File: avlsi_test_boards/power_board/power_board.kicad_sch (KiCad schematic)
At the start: 4 parts, among them J1 PJ-102AH, J2 PJ-102AH, J3 Conn_02x06_Top_Bottom, J4 Conn_02x06_Top_Bottom

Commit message: Fully routed
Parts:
- removed J3, J4: Conn_02x06_Top_Bottom, Connector_PinHeader_2.54mm:PinHeader_2x06_P2.54mm_Vertical, symbol Connector_Generic:Conn_02x06_Top_Bottom
- added J3, J9: Conn_02x07_Top_Bottom, Connector_PinHeader_2.00mm:PinHeader_2x07_P2.00mm_Vertical, symbol Connector_Generic:Conn_02x07_Top_Bottom
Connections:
- net DGND: now also J9.1 (Pin_1), J9.11 (Pin_11), J9.13 (Pin_13), J9.3 (Pin_3), J9.5 (Pin_5), J9.7 (Pin_7), J9.9 (Pin_9)
- net VCCA09: now also J3.12 (Pin_12)
- net VCCA12: now also J3.10 (Pin_10)
- net VCCA18: now also J3.8 (Pin_8)
- net VCCA25: now also J3.6 (Pin_6)
- net VCCA33: now also J3.4 (Pin_4)
- net VCCD09: now also J9.4 (Pin_4)
- net VCCD12: now also J9.6 (Pin_6)
- net VCCD18: now also J9.8 (Pin_8)
- net VCCD25: now also J9.10 (Pin_10)
- net VCCD33: now also J9.12 (Pin_12)
- net AGND renamed ADGND
- net ADGND: now also J3.1 (Pin_1), J3.11 (Pin_11), J3.13 (Pin_13), J3.3 (Pin_3), J3.5 (Pin_5), J3.7 (Pin_7), J3.9 (Pin_9)
- net AVIN renamed AVIN5
- net AVIN5: now also J3.2 (Pin_2)
- net DVIN renamed DVIN5
- net DVIN5: now also J9.14 (Pin_14)
- new net VACustom: J3.14 (Pin_14)
- new net VDCustom: J9.2 (Pin_2)
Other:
- sheet analog_power_converters ports: added DGND; removed GND
- sheet digital_power_converters ports: added DGND; removed GND

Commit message: Add partial changes
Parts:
- removed J3, J9: Conn_02x07_Top_Bottom, Connector_PinHeader_2.00mm:PinHeader_2x07_P2.00mm_Vertical, symbol Connector_Generic:Conn_02x07_Top_Bottom
- added J3, J7: Conn_02x07_Odd_Even, Connector_PinHeader_2.54mm:PinHeader_2x07_P2.54mm_Vertical, symbol Connector_Generic:Conn_02x07_Odd_Even
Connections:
- net ADGND: now also J3.10 (Pin_10), J3.12 (Pin_12), J3.14 (Pin_14), J3.2 (Pin_2), J3.4 (Pin_4), J3.6 (Pin_6), J3.8 (Pin_8)
- net AVIN5: now also J3.13 (Pin_13)
- net DGND: now also J7.10 (Pin_10), J7.12 (Pin_12), J7.14 (Pin_14), J7.2 (Pin_2), J7.4 (Pin_4), J7.6 (Pin_6), J7.8 (Pin_8)
- net DVIN5: now also J7.13 (Pin_13)
- net VACustom: now also J3.1 (Pin_1)
- net VCCA09: now also J3.3 (Pin_3)
- net VCCA12: now also J3.5 (Pin_5)
- net VCCA18: now also J3.7 (Pin_7)
- net VCCA25: now also J3.9 (Pin_9)
- net VCCA33: now also J3.11 (Pin_11)
- net VCCD09: now also J7.3 (Pin_3)
- net VCCD12: now also J7.5 (Pin_5)
- net VCCD18: now also J7.7 (Pin_7)
- net VCCD25: now also J7.9 (Pin_9)
- net VCCD33: now also J7.11 (Pin_11)
- net VDCustom: now also J7.1 (Pin_1)
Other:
- added sheet level_shifter (level_shifter.kicad_sch)
- added sheet opal_kelly_connector (opal_kelly_connector.kicad_sch)

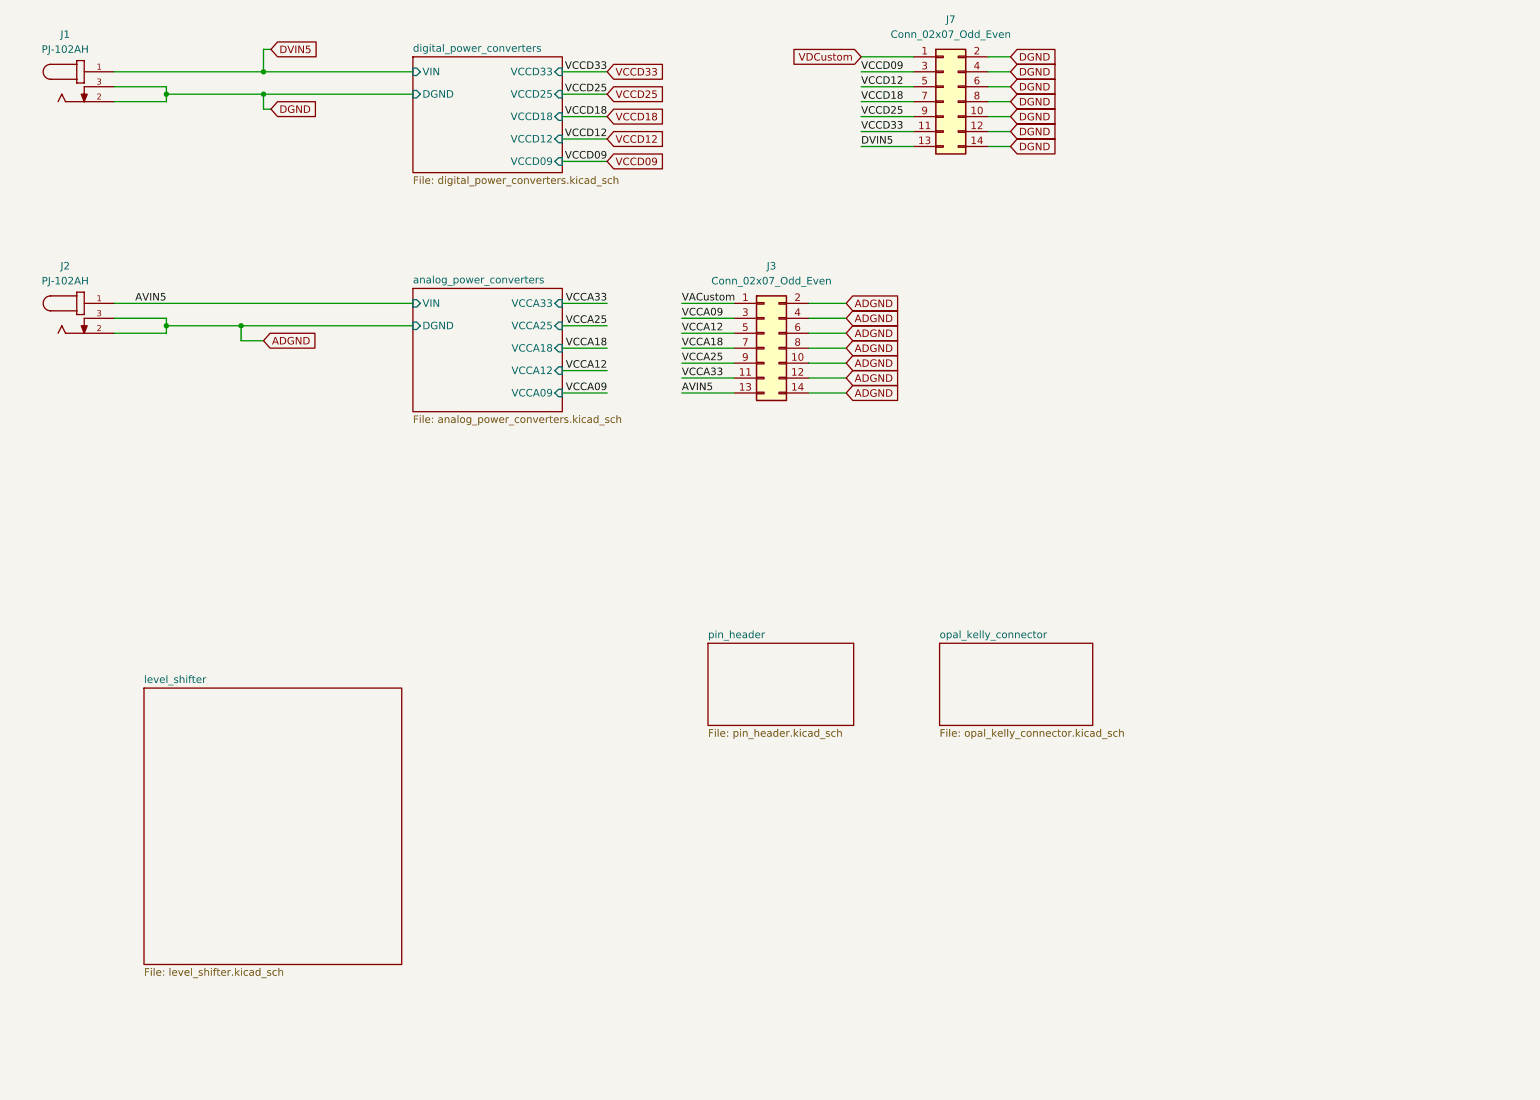
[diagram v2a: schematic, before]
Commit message: Add updated schematic
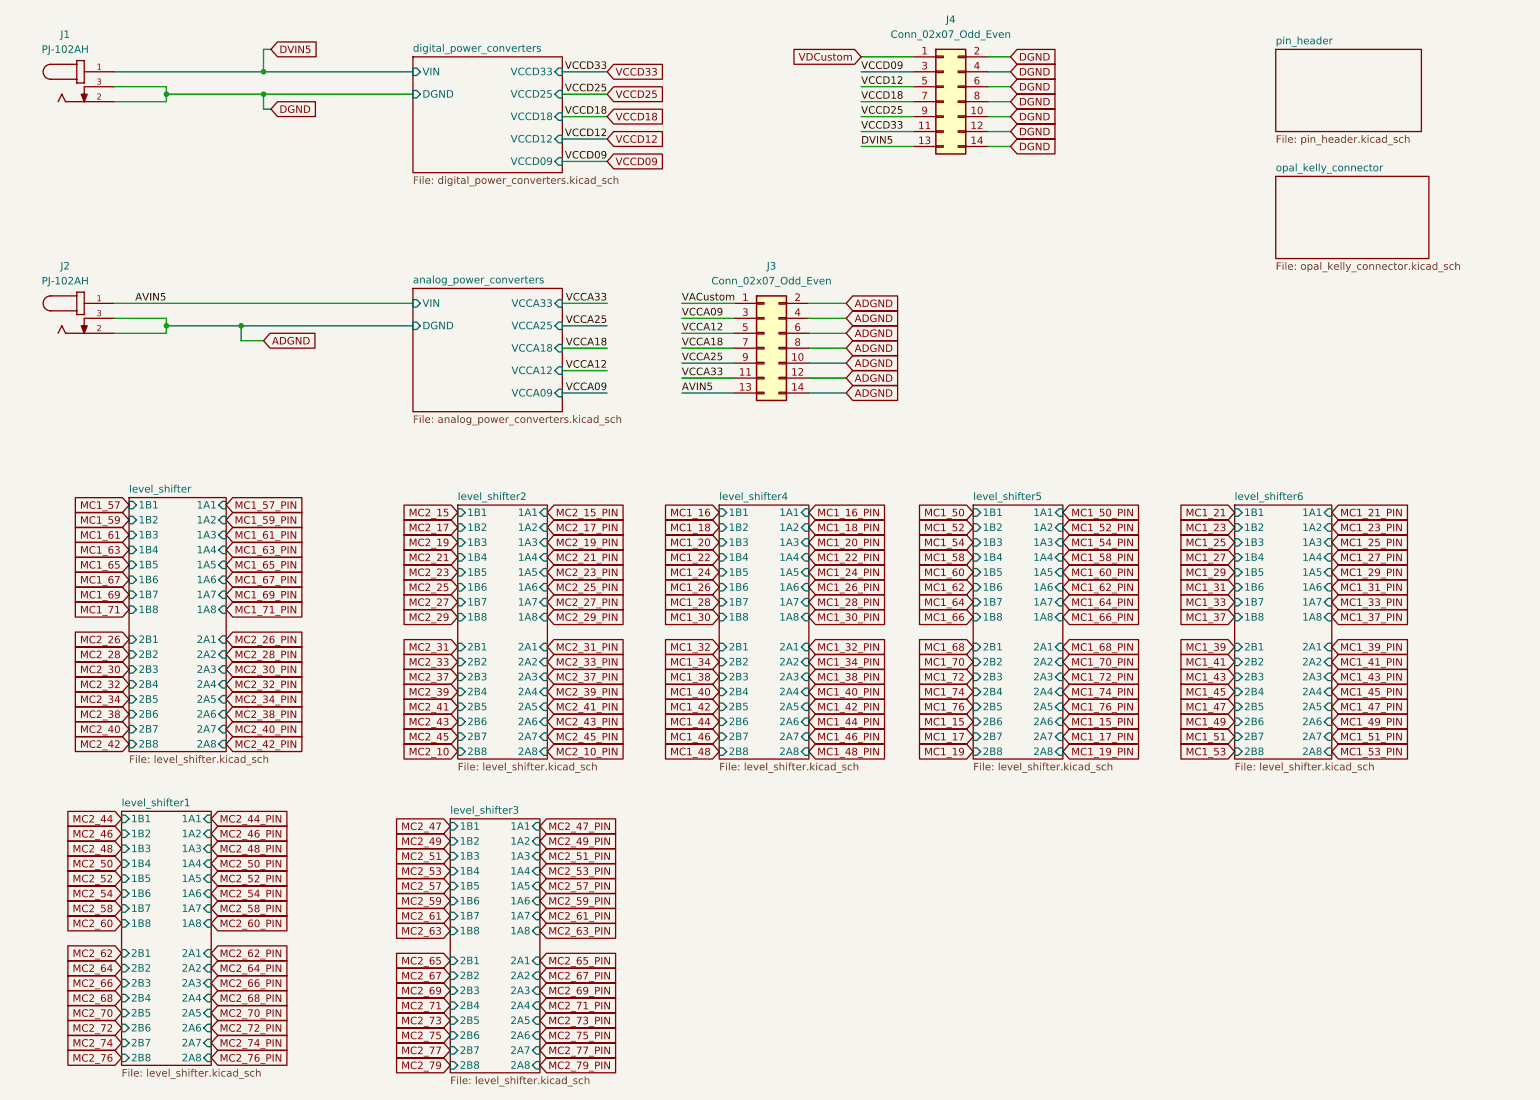
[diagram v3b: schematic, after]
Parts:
- renumbered J7 to J4
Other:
- added sheet level_shifter1 (level_shifter.kicad_sch)
- added sheet level_shifter2 (level_shifter.kicad_sch)
- added sheet level_shifter3 (level_shifter.kicad_sch)
- added sheet level_shifter4 (level_shifter.kicad_sch)
- added sheet level_shifter5 (level_shifter.kicad_sch)
- added sheet level_shifter6 (level_shifter.kicad_sch)
- sheet level_shifter ports: added 1A1, 1A2, 1A3, 1A4, 1A5, 1A6, 1A7, 1A8, 1B1, 1B2, 1B3, 1B4, 1B5, 1B6, 1B7, 1B8, 2A1, 2A2, 2A3, 2A4, 2A5, 2A6, 2A7, 2A8, 2B1, 2B2, 2B3, 2B4, 2B5, 2B6, 2B7, 2B8; removed none

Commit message: Add initial layout stuff
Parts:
- added J10, J9: Conn_02x07_Odd_Even, Connector_PinHeader_2.54mm:PinHeader_2x07_P2.54mm_Vertical, symbol Connector_Generic:Conn_02x07_Odd_Even
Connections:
- net ADGND: now also J9.10 (Pin_10), J9.12 (Pin_12), J9.14 (Pin_14), J9.2 (Pin_2), J9.4 (Pin_4), J9.6 (Pin_6), J9.8 (Pin_8)
- net AVIN5: now also J9.13 (Pin_13)
- net DGND: now also J10.10 (Pin_10), J10.12 (Pin_12), J10.14 (Pin_14), J10.2 (Pin_2), J10.4 (Pin_4), J10.6 (Pin_6), J10.8 (Pin_8)
- net DVIN5: now also J10.13 (Pin_13)
- net VACustom: now also J9.1 (Pin_1)
- net VCCA09: now also J9.3 (Pin_3)
- net VCCA12: now also J9.5 (Pin_5)
- net VCCA18: now also J9.7 (Pin_7)
- net VCCA25: now also J9.9 (Pin_9)
- net VCCA33: now also J9.11 (Pin_11)
- net VCCD09: now also J10.3 (Pin_3)
- net VCCD12: now also J10.5 (Pin_5)
- net VCCD18: now also J10.7 (Pin_7)
- net VCCD25: now also J10.9 (Pin_9)
- net VCCD33: now also J10.11 (Pin_11)
- net VDCustom: now also J10.1 (Pin_1)

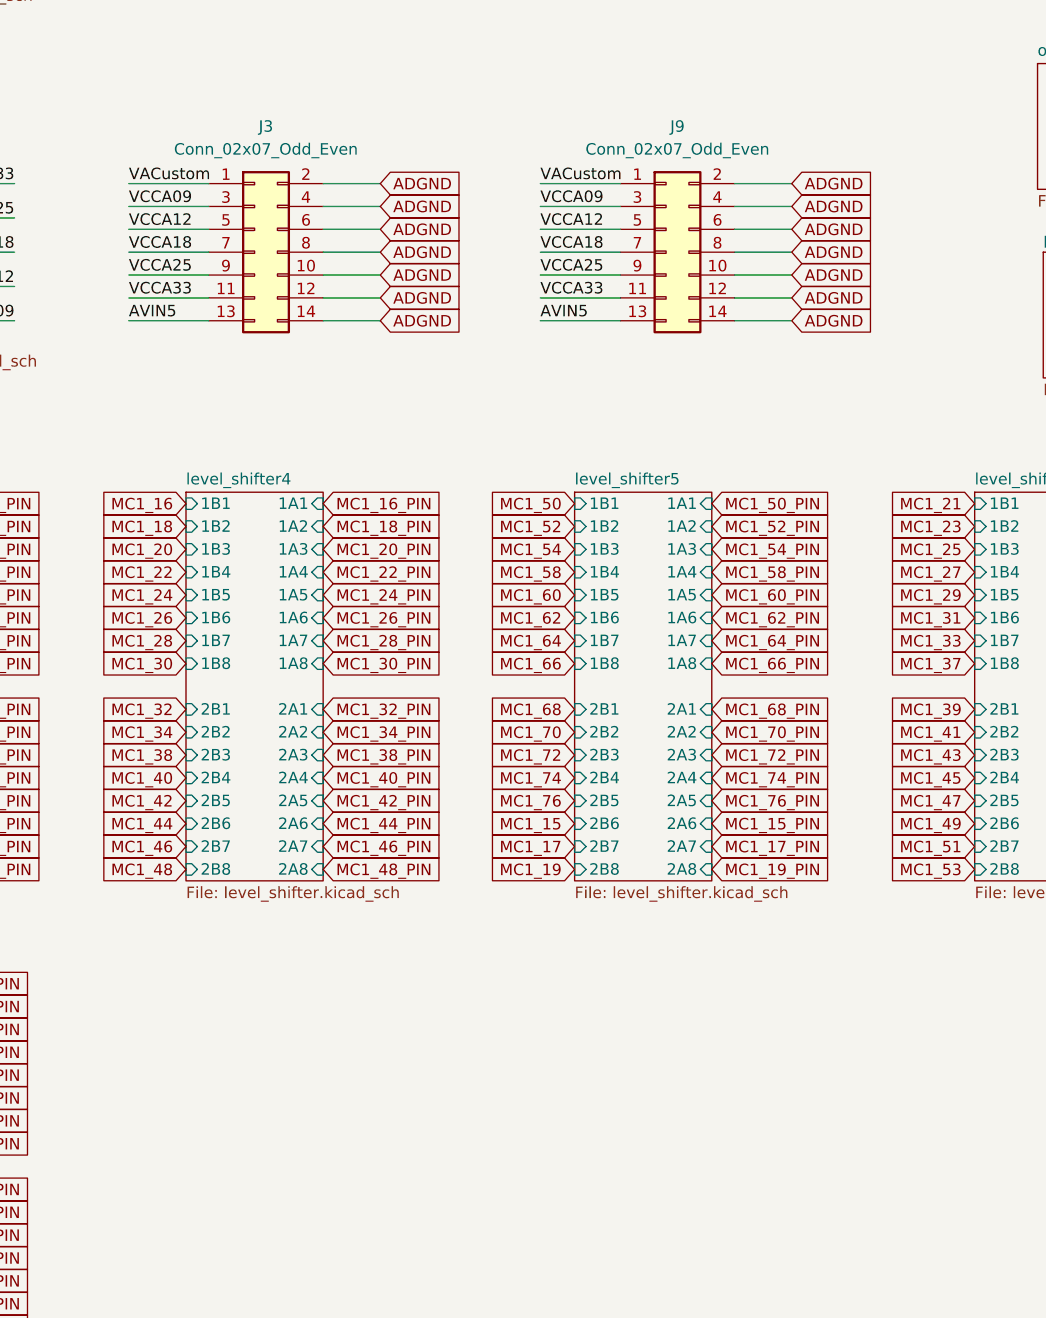
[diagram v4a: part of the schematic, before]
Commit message: Add analog power pins
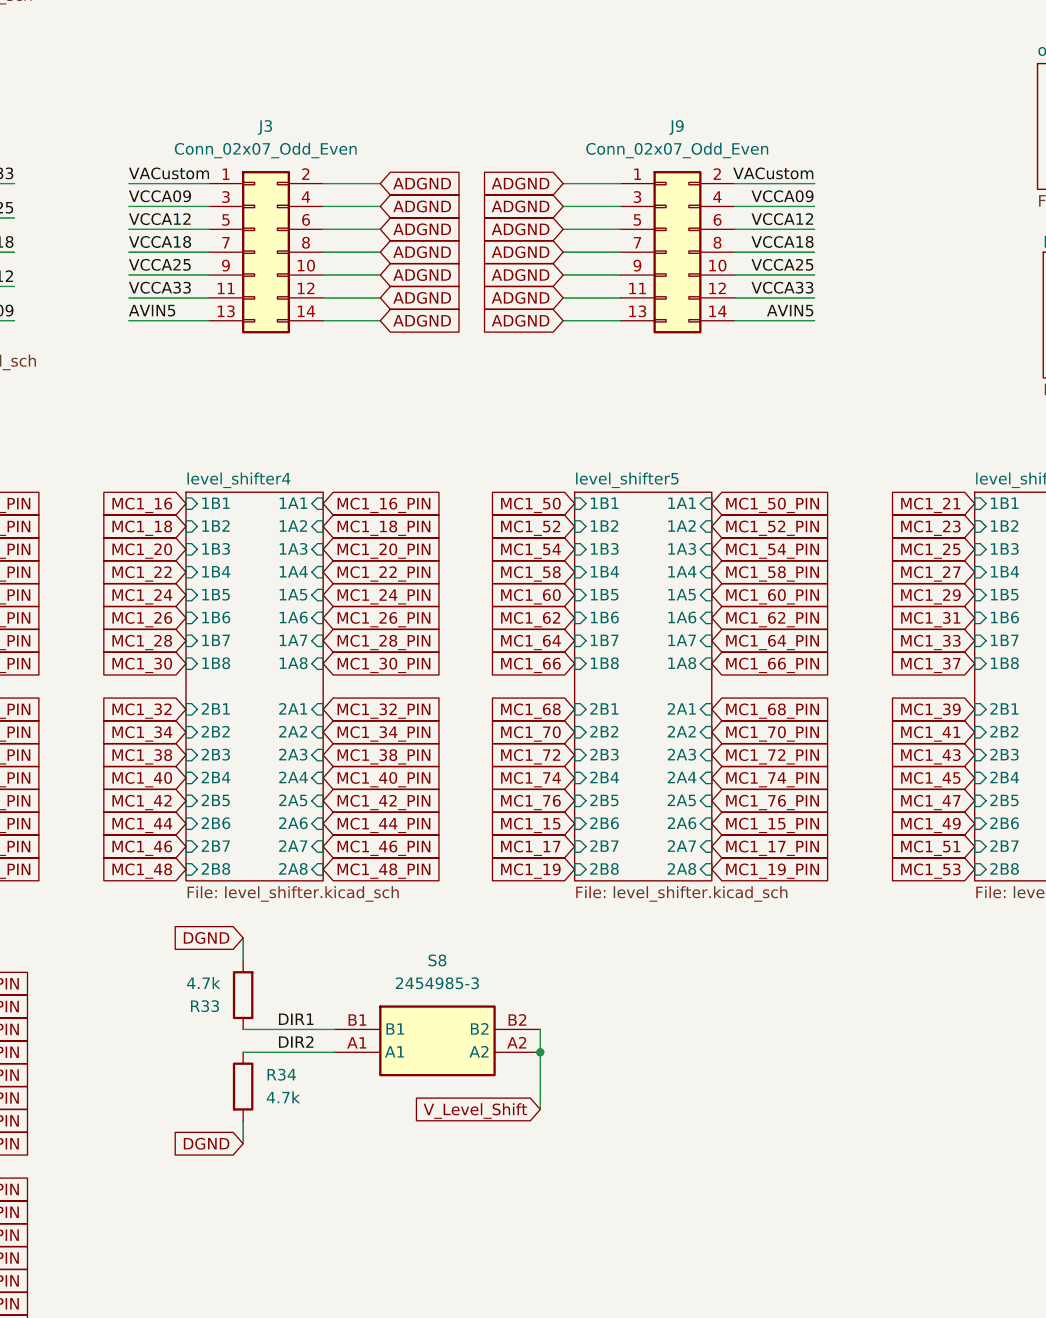
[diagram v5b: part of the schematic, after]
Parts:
- added R33, R34: 4.7k, Resistor_SMD:R_0805_2012Metric, symbol Device:R
- added S8: 2454985-3, 2_DS:24549853, symbol 2_DIP:2454985-3
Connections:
- net ADGND: now also J9.1 (Pin_1), J9.11 (Pin_11), J9.13 (Pin_13), J9.3 (Pin_3), J9.5 (Pin_5), J9.7 (Pin_7), J9.9 (Pin_9); no longer J9.10 (Pin_10), J9.12 (Pin_12), J9.14 (Pin_14), J9.2 (Pin_2), J9.4 (Pin_4), J9.6 (Pin_6), J9.8 (Pin_8)
- net AVIN5: now also J9.14 (Pin_14); no longer J9.13 (Pin_13)
- net DGND: now also R33.2, R34.2
- net VACustom: now also J9.2 (Pin_2); no longer J9.1 (Pin_1)
- net VCCA09: now also J9.4 (Pin_4); no longer J9.3 (Pin_3)
- net VCCA12: now also J9.6 (Pin_6); no longer J9.5 (Pin_5)
- net VCCA18: now also J9.8 (Pin_8); no longer J9.7 (Pin_7)
- net VCCA25: now also J9.10 (Pin_10); no longer J9.9 (Pin_9)
- net VCCA33: now also J9.12 (Pin_12); no longer J9.11 (Pin_11)
- new net DIR1: R33.1, S8.B1
- new net DIR2: R34.1, S8.A1
- new net V_Level_Shift: S8.A2, S8.B2
